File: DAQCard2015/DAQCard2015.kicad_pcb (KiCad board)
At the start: 4 copper layers, 160 x 160 mm, 188 parts, among them CON1 BARREL_JACK, K1 1462042-8, P1 QTH-090-01-F-D-A, P2 QTH-090-01-F-D-A, P3 miniDIL20, P4 LEMO_EPY.00.250.NTN, P5 LEMO_EPY.00.250.NTN, P6 FAN, P7 CONN_02X20_Double, P9 SHV, Q1 Q_NPN_BCE, Q2 NPN, SW1 DPDT, U1 RJ45x8, U10 AD9219, U11 THS4524IDBTR, U12 AD9219, U13 THS4524IDBTR, U14 AD9219, U15 THS4524IDBTR, U16 AD9219, U17 THS4524IDBTR, U18 AD9219, U2 AD5628, U20 LM1086, U21 LT1913, U24 MCP65R41, U3 THS4524IDBTR, U4 AD9219, U5 THS4524IDBTR, U6 AD9219, U7 THS4524IDBTR, U8 AD9219, U9 THS4524IDBTR

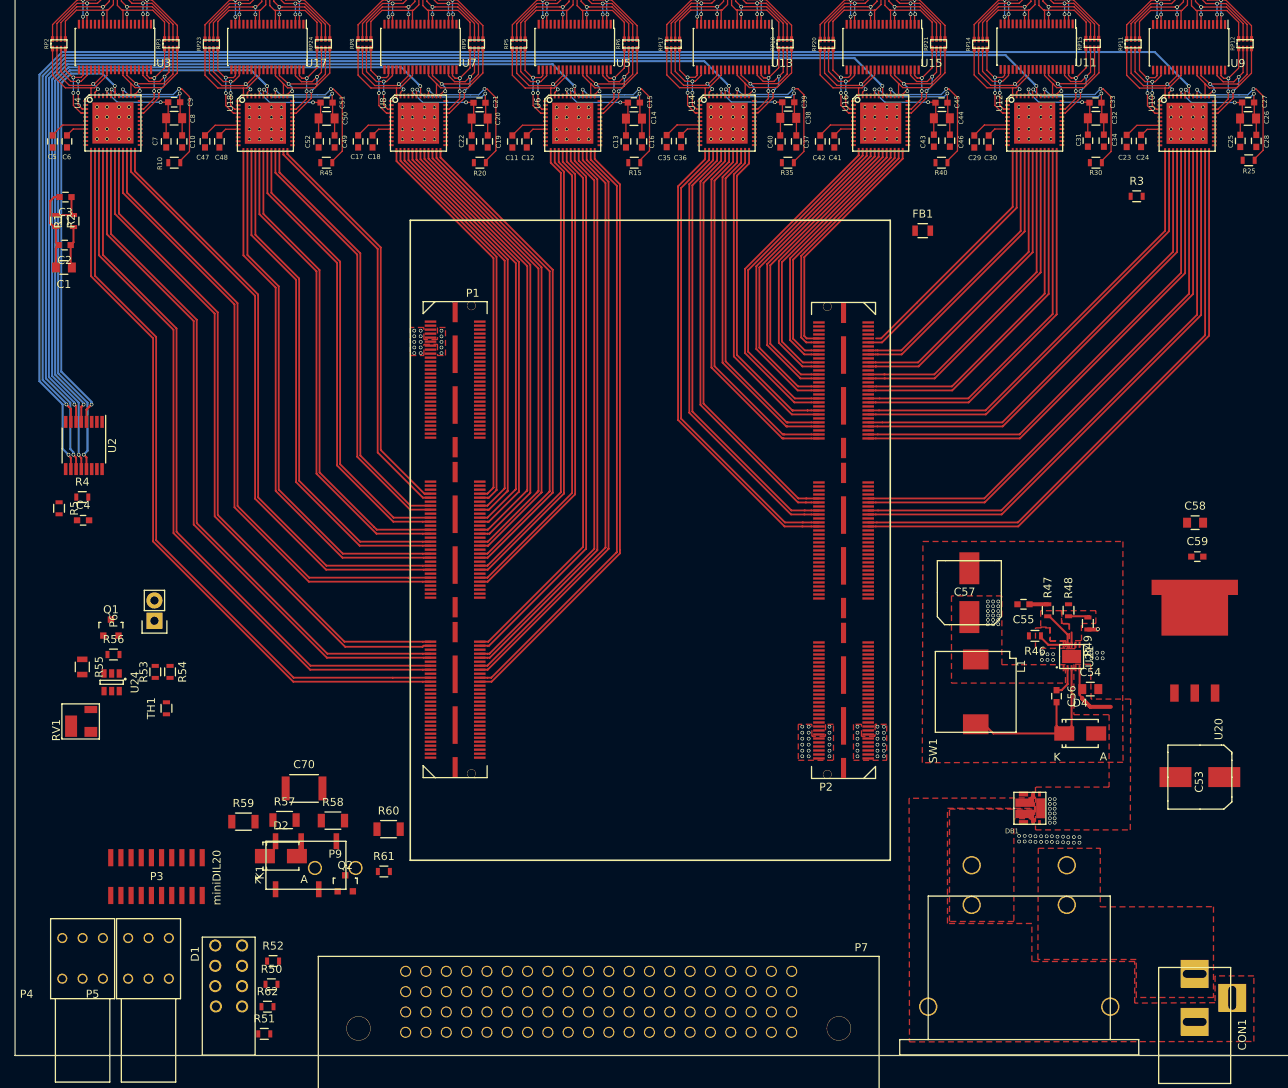
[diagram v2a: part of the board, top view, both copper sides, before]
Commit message: Updates to DAQ board focusing on Support electronics
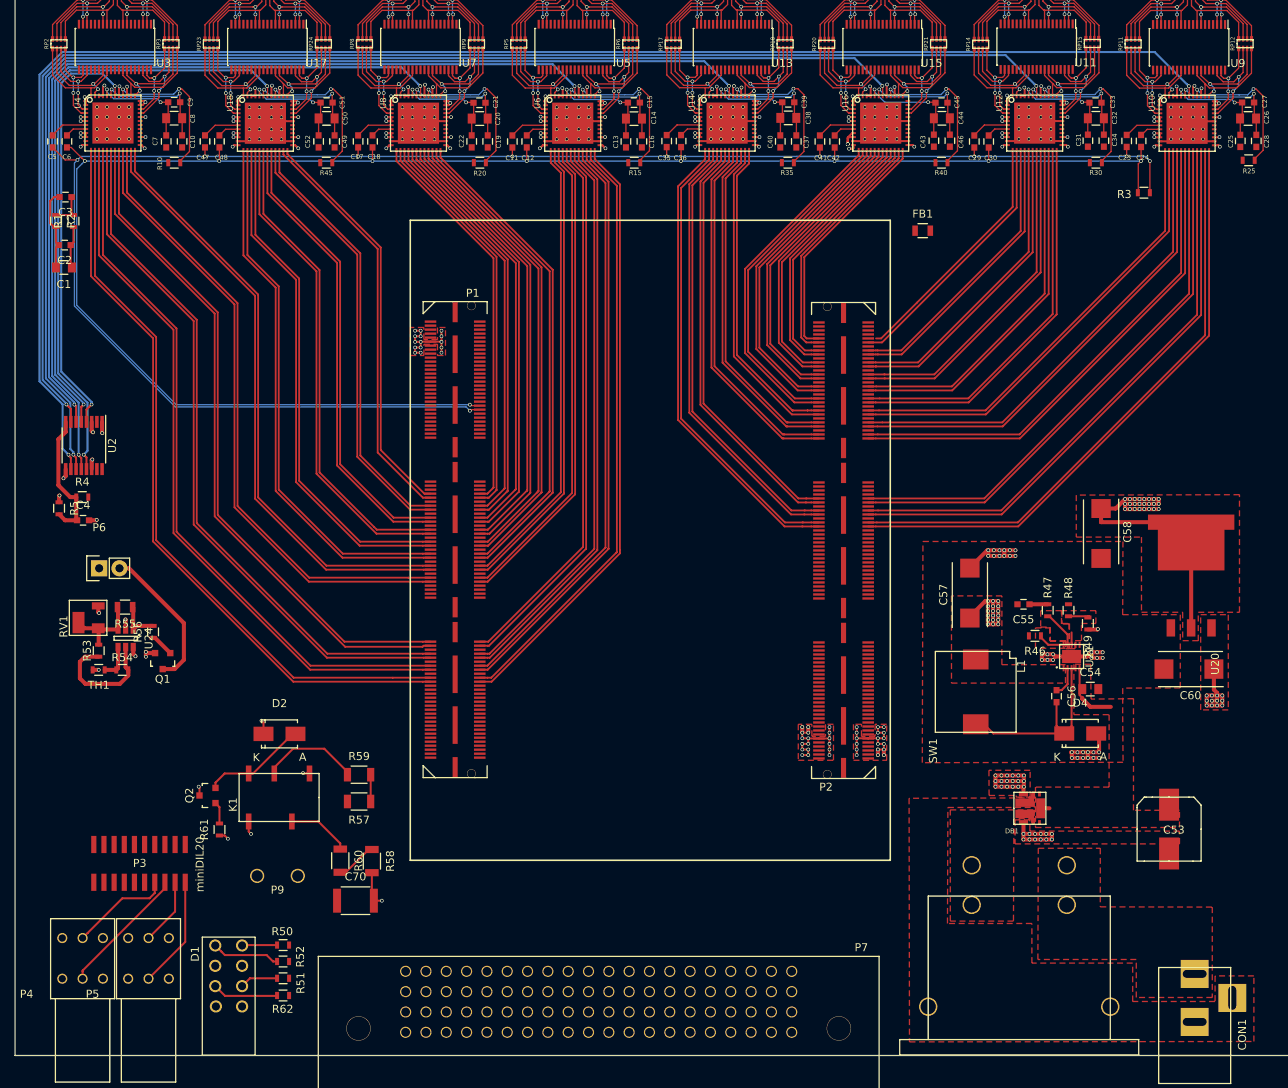
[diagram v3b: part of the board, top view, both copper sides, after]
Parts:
- removed C59: .1uF, Capacitors_SMD:C_0603
- added C60: 10uF, Capacitors_Tantalum_SMD:TantalC_SizeD_EIA-7343_Reflow, F.Cu at (164.7, 135.9)
- C57: footprint extras:SMD_Cap_8mmDia -> Capacitors_Tantalum_SMD:TantalC_SizeD_EIA-7343_Reflow
- C58: value 10uF -> 100uF; footprint Capacitors_SMD:C_0805 -> Capacitors_Tantalum_SMD:TantalC_SizeD_EIA-7343_Reflow
- Q1: value Q_NPN_BCE -> Q_NPN_BCE_REV
- moved R61 21.2 mm to (43.5, 155.9), turned to 90 degrees
- moved Q2 20.4 mm to (42.0, 151.7), turned to 90 degrees
- moved R59 15.6 mm to (61.0, 149.1)
- moved C70 15.4 mm to (60.5, 164.8)
- moved D2 15.3 mm to (51.0, 144.0)
- moved RV1 13.0 mm to (28.4, 129.4)
- moved C58 11.8 mm to (153.8, 119.0), turned to 270 degrees
- moved TH1 9.74 mm to (28.4, 136.0), turned to 180 degrees
- moved R57 9.60 mm to (61.0, 152.4), turned to 180 degrees
- moved P6 9.53 mm to (28.5, 123.3), turned to 0 degrees
- moved R55 9.20 mm to (31.8, 128.2), turned to 180 degrees
- moved K1 9.11 mm to (51.0, 151.9)
- moved U20 8.16 mm to (165.0, 130.8)
- moved Q1 7.71 mm to (36.5, 134.9), turned to 180 degrees
- moved C53 7.55 mm to (162.2, 155.9), turned to 0 degrees
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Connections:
- net /Frontend/ADCChannel1/Vocm renamed Vocm
- net /Frontend/Aref renamed Aref
- net /Frontend/CAL renamed CAL
- net /Frontend/CS renamed CS
- net /Frontend/IS1 renamed IS1
- net /Frontend/IS2 renamed IS2
- net /Frontend/LE renamed LE
- net /Frontend/NULL renamed NULL
- net /Frontend/R12 renamed R12
- net /Frontend/RBI renamed RBI
- net /Frontend/RG renamed RG
- net /Frontend/RPHI1 renamed RPHI1
- net /Frontend/RPHI2 renamed RPHI2
- net /Frontend/Reset renamed Reset
- net /Frontend/SBI renamed SBI
- net /Frontend/SCL renamed SCL
- net /Frontend/SDA renamed SDA
- net /Frontend/SEB renamed SEB
- net /Frontend/SPHI1 renamed SPHI1
- net /Frontend/SPHI2 renamed SPHI2
- net /Frontend/SR renamed SR
- net /Frontend/Vdig renamed Vdig
- net /Frontend/Vthresh renamed Vthresh
- C70 pad 2: /MISCIO/Vbias -> Vbias
- P1 pad 43: (no net) -> ADC_CLK+
- P1 pad 45: (no net) -> ADC_CLK-
- P4 pad 1: Net-(P3-Pad8) -> Net-(P3-Pad6)
- P4 pad 2: Net-(P3-Pad6) -> Net-(P3-Pad8)
- P5 pad 1: Net-(P3-Pad4) -> Net-(P3-Pad2)
- P5 pad 2: Net-(P3-Pad2) -> Net-(P3-Pad4)
- P7 pad 1: /Frontend/Vbias -> Vbias
- P7 pad 28: /Frontend/RBO1 -> (no net)
- P7 pad 29: /Frontend/RBO2 -> (no net)
- P7 pad 30: /Frontend/RBO3 -> (no net)
- P7 pad 31: /Frontend/RBO4 -> (no net)
- P7 pad 41: /Frontend/Vbias -> Vbias
- P7 pad 68: /Frontend/RBO1 -> (no net)
- P7 pad 69: /Frontend/RBO2 -> (no net)
- P7 pad 70: /Frontend/RBO3 -> (no net)
- P7 pad 71: /Frontend/RBO4 -> (no net)
- Q1 pad 2: Net-(P6-Pad2) -> GND
- Q1 pad 3: GND -> Net-(P6-Pad2)
- R58 pad 2: /MISCIO/Vbias -> Vbias
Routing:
- net ADC_CLK-: track 0.00 -> 236.2 mm, vias 0 -> 10
- net ADC_CLK+: track 0.00 -> 225.2 mm, vias 0 -> 9
- net 1V8ana: track 0.00 -> 133.8 mm, vias 0 -> 109
- net GND: track 11.4 -> 114.2 mm, vias 0 -> 77
- net Vbias: track 0.00 -> 65.4 mm, vias 0 -> 1
- net 5Vdig: track 1.64 -> 59.0 mm, vias 1 -> 69
- net 1V8dig: track 0.00 -> 24.3 mm, vias 0 -> 31
- net Net-(K1-Pad5): track 0.00 -> 19.0 mm, vias 0 -> 1
- net Net-(P6-Pad2): track 0.00 -> 18.6 mm
- net Net-(C4-Pad1): track 0.00 -> 16.6 mm
- net Net-(P3-Pad6): track 0.00 -> 16.3 mm
- net Net-(R53-Pad1): track 0.00 -> 15.1 mm
- net Net-(P3-Pad2): track 0.00 -> 14.0 mm
- net Net-(D2-Pad2): track 0.00 -> 13.2 mm
- net Net-(P3-Pad8): track 0.00 -> 12.7 mm
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- added copper zone on F.Cu, net 1V8ana
- added copper zone on POWER.Cu, net 1V8ana
- added copper zone on POWER.Cu, net 1V8dig

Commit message: Adds APC128 connections and voltage supplies
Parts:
- added U19: AD8534, Housings_SSOP:TSSOP-14_4.4x5mm_Pitch0.65mm, F.Cu at (91.0, 136.8)
- added U22: AD5628, extras:TSSOP-16_4.4x5mm_Pitch0.65mm, F.Cu at (98.2, 128.7)
- added U23: AD8534, Housings_SSOP:TSSOP-14_4.4x5mm_Pitch0.65mm, F.Cu at (105.5, 136.8)
- D2: value D -> SMAJ75A
- Q1: value Q_NPN_BCE_REV -> MMBT2222A-TP
- Q2: value NPN -> SBC817-40LT1G
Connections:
- P1 pad 145: (no net) -> IS1
- P1 pad 146: (no net) -> SCL
- P1 pad 147: (no net) -> Reset
- P1 pad 148: /ZEM4310/H1_LVDS_RXn13 -> SDA
- P1 pad 151: (no net) -> LE
- P1 pad 152: (no net) -> RPHI1
- P1 pad 153: (no net) -> SPHI2
- P1 pad 154: /ZEM4310/H1_LVDS_RXn13 -> RPHI2
- P1 pad 157: (no net) -> SPHI1
- P1 pad 158: (no net) -> RBO_A4
- P1 pad 159: (no net) -> SBI
- P1 pad 160: (no net) -> RBO_B4
- P1 pad 163: (no net) -> SEB
- P1 pad 164: (no net) -> RBO_B3
- P1 pad 165: (no net) -> CAL
- P1 pad 166: (no net) -> RBO_B2
- P1 pad 169: (no net) -> RBO_A1
- P1 pad 170: (no net) -> RBO_A2
- P1 pad 171: (no net) -> RBO_B1
- P1 pad 172: (no net) -> RBO_A3
- P2 pad 67: (no net) -> RBI
- P2 pad 69: (no net) -> CS
- P2 pad 73: (no net) -> R12
- P2 pad 75: (no net) -> SR
- P2 pad 79: (no net) -> IS2
- P7 pad 16: RG -> RG_A
- P7 pad 28: (no net) -> RBO_A1
- P7 pad 29: (no net) -> RBO_A2
- P7 pad 30: (no net) -> RBO_A3
- P7 pad 31: (no net) -> RBO_A4
- P7 pad 34: Aref -> Aref_A
- P7 pad 4: Vana -> Vana_A
- P7 pad 44: Vana -> Vana_B
- P7 pad 45: Vana -> Vana_B
- P7 pad 5: Vana -> Vana_A
- P7 pad 56: RG -> RG_B
- P7 pad 68: (no net) -> RBO_B1
- P7 pad 69: (no net) -> RBO_B2
- P7 pad 70: (no net) -> RBO_B3
- P7 pad 71: (no net) -> RBO_B4
- P7 pad 74: Aref -> Aref_B
- Q2 pad 2: Net-(D2-Pad2) -> GND
- Q2 pad 3: GND -> Net-(D2-Pad2)
- U2 pad 15: (no net) -> SPI_SDIO
- U2 pad 16: (no net) -> SPI_SCLK
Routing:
- net IS2: track 0.00 -> 71.6 mm
- net CS: track 0.00 -> 67.5 mm
- net SR: track 0.00 -> 67.2 mm
- net R12: track 0.00 -> 66.7 mm
- net RBI: track 0.00 -> 66.1 mm
- net Aref_B: track 0.00 -> 53.1 mm, vias 0 -> 1
- net Vocm: track 9.74 -> 61.8 mm, vias 0 -> 1
- net Reset: track 0.00 -> 51.3 mm
- net Vthresh: track 0.00 -> 50.7 mm, vias 0 -> 1
- net IS1: track 0.00 -> 50.0 mm
- net Vana_B: track 0.00 -> 49.7 mm, vias 0 -> 1
- net Aref_A: track 0.00 -> 49.5 mm, vias 0 -> 1
- net SCL: track 0.00 -> 49.5 mm
- net RPHI2: track 0.00 -> 49.2 mm
- net RG_B: track 0.00 -> 49.0 mm, vias 0 -> 1
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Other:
- net class HV added: clearance 0.508, trace_width 0.1524, via_dia 0.4572, via_drill 0.3048
